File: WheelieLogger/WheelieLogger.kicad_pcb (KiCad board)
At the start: 2 copper layers, 28.8 x 22 mm, 34 parts, among them J1 USB_C_Plug_USB2.0, J2 Conn_Power, J3 Conn_GPIO, SW1 SW_RESET, U1 GD25Q32CNIGR, U2 MCP1700-3302E_SOT23, U3 ATSAMD21E18A, U4 MPU-6050

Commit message: Draft of SerpenteR2 board instructions
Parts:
- removed J3: Conn_GPIO, Connector_PinHeader_2.54mm_Extra:PinHeader_1x06_P2.54mm_Vertical_Castellated
- added SW2: SW_DIP_x02, Package_DIP:SMDIP-4_W7.62mm, F.Cu at (155.0, 88.3)
- J2: footprint Connector_PinHeader_2.54mm_Extra:PinHeader_1x04_P2.54mm_Vertical_Castellated -> Connector_JST:JST_PH_B2B-PH-SM4-TB_1x02-1MP_P2.00mm_Vertical
- moved R5 13.8 mm to (151.4, 78.7), turned to 180 degrees
- moved D3 11.0 mm to (142.1, 98.0)
- moved R1 11.0 mm to (140.6, 95.0)
- moved R2 11.0 mm to (142.1, 95.0)
- moved R3 11.0 mm to (143.6, 95.0)
- moved R7 10.8 mm to (151.4, 80.2)
- moved J2 6.94 mm to (155.0, 96.0), turned to 0 degrees
- moved D2 6.63 mm to (146.8, 98.0)
- moved D1 6.54 mm to (146.8, 96.0)
- moved C8 6.29 mm to (158.6, 81.8), turned to -90 degrees
- moved C6 4.22 mm to (151.4, 81.7), turned to 180 degrees
- moved C5 3.61 mm to (151.4, 84.7), turned to 0 degrees
- moved C7 3.17 mm to (151.4, 83.2), turned to 180 degrees
- moved U4 2.44 mm to (155.2, 81.5), turned to -90 degrees
- moved C1 1.92 mm to (147.7, 94.0), turned to 180 degrees
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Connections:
- J2 pad 1: VIN -> /PWR_SW
- J2 pad 2: VBUS -> GND
- U3 pad 5: /GPIO0 -> Net-(U3-Pad5)
- U3 pad 6: /GPIO1 -> Net-(U3-Pad6)
- U3 pad 7: /GPIO2 -> Net-(U3-Pad7)
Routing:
- net Net-(U3-Pad5): track 0.00 -> 10.9 mm
- net /GPIO0: track 10.9 -> 0.00 mm
- net /PWR_SW: track 0.00 -> 10.3 mm
- net VIN: track 9.98 -> 0.00 mm
- net /LED_B: track 23.1 -> 33.1 mm
- net Net-(U3-Pad7): track 0.00 -> 9.39 mm
- net /GPIO2: track 9.39 -> 0.00 mm
- net Net-(U3-Pad6): track 0.00 -> 9.30 mm
- net /GPIO1: track 9.30 -> 0.00 mm
- net GND: track 23.1 -> 15.2 mm
- net +3V3: track 63.9 -> 61.5 mm
- net Net-(C7-Pad1): vias 0 -> 1
- net /GPIO4: vias 1 -> 0

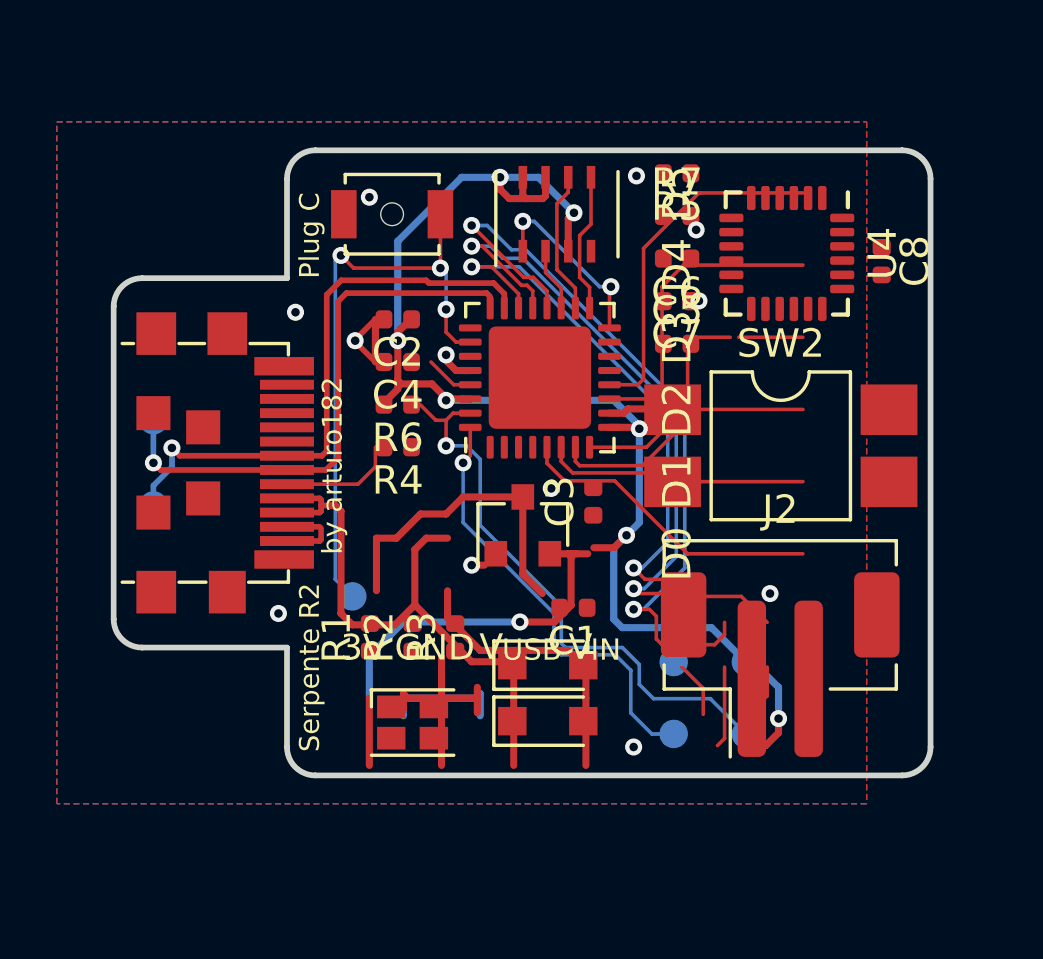
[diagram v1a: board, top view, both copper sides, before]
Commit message: 1.Added 1uF cap to pin2 of the MCP1700 (U2) 2.Removed dip switches, replaced with DPDT slide switch as they should always operate together 3.Updated the JST-PH connector from an SMD to a through-hole unit 4.Updated the footprint of the USB-C connector
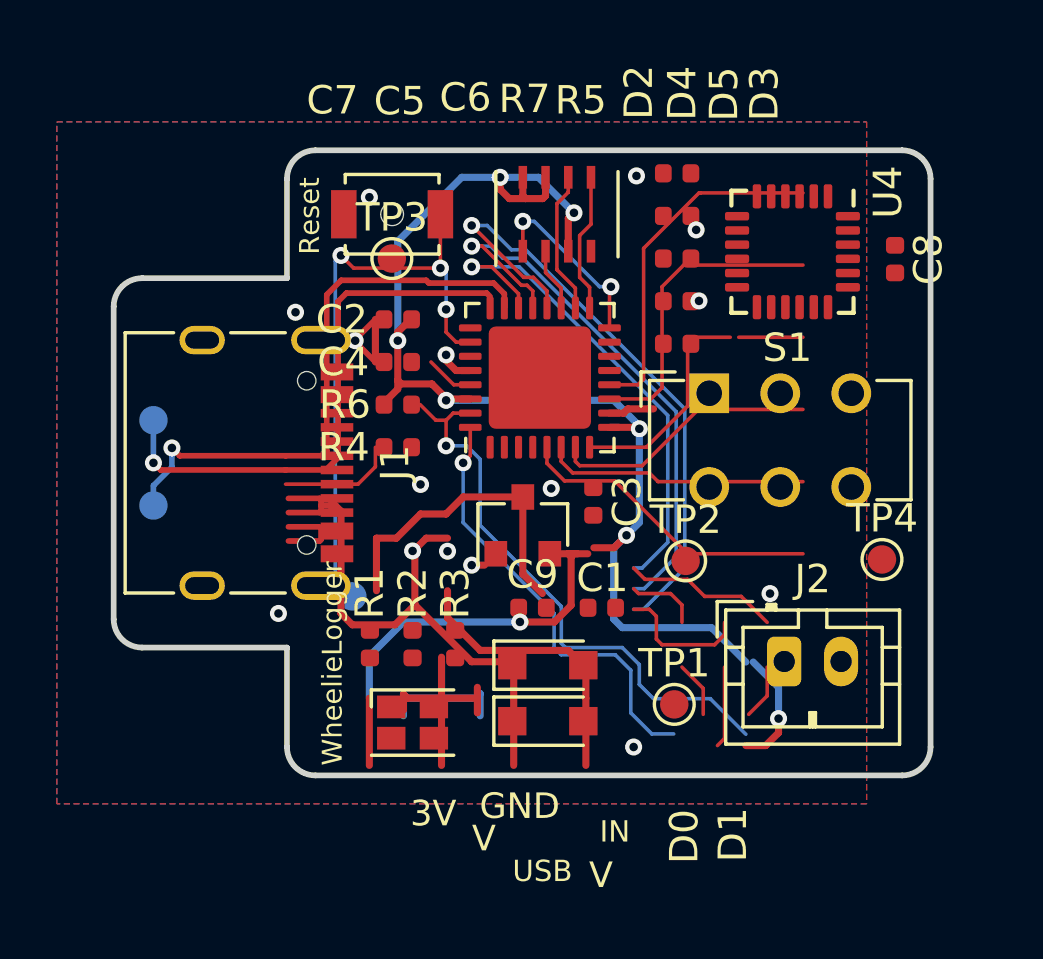
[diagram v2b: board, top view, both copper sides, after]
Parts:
- removed SW2: SW_DIP_x02, Package_DIP:SMDIP-4_W7.62mm
- added C9: 1uF, Capacitor_SMD:C_0402_1005Metric, F.Cu at (146.3, 94.0)
- added S1: JS202011JCQN, Button_Switch_THT:SW_CuK_JS202011CQN_DPDT_Straight, F.Cu at (152.5, 86.5)
- J1: footprint Connector_USB_Extra:USB_C_Plug_UTC009-C12 -> Connector_USB:USB_C_Receptacle_XKB_U262-16XN-4BVC11
- J2: footprint Connector_JST:JST_PH_B2B-PH-SM4-TB_1x02-1MP_P2.00mm_Vertical -> Connector_JST:JST_PH_B2B-PH-K_1x02_P2.00mm_Vertical
- TP1, TP2, TP3, TP4: moved to F.Cu
- moved TP3 18.9 mm to (141.3, 81.7), turned to 0 degrees
- moved TP4 8.17 mm to (158.6, 92.3), turned to 0 degrees
- moved TP2 6.10 mm to (151.7, 92.3), turned to 0 degrees
- moved TP1 2.73 mm to (151.3, 97.4), turned to 0 degrees
- moved J1 1.71 mm to (135.7, 88.9)
- moved C1 1.00 mm to (148.7, 94.0)
- moved C8 0.48 mm to (159.1, 81.7)
- moved R1 0.24 mm to (140.6, 95.3)
- moved R2 0.24 mm to (142.1, 95.3)
- moved R3 0.24 mm to (143.6, 95.3)
- moved U4 0.21 mm to (155.4, 81.5)
- moved J2 0.18 mm to (155.2, 95.9)
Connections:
- U2 pad 2: +3V3 -> Net-(C9-Pad2)
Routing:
- net +3V3: track 61.5 -> 44.6 mm, vias 9 -> 7
- net /PWR_SW: track 10.3 -> 24.5 mm, vias 0 -> 2
- net Net-(C9-Pad2): track 0.00 -> 12.8 mm, vias 0 -> 1
- net /LED_B: track 33.1 -> 27.6 mm
- net VBUS: track 21.3 -> 24.0 mm
- net GND: track 15.2 -> 12.5 mm, vias 10 -> 9
- net /LED_R: track 22.6 -> 20.1 mm, vias 2 -> 1
- net Net-(D3-Pad2): track 1.93 -> 0.00 mm
- net +5V: vias 0 -> 1
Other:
- board text added: "Reset"
- board text added: "WheelieLogger"
- board text removed: "Plug C"
- board text removed: "Serpente R2"
- board text removed: "by arturo182"

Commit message: Rebuilt the tracks in the PCB Removed some test points
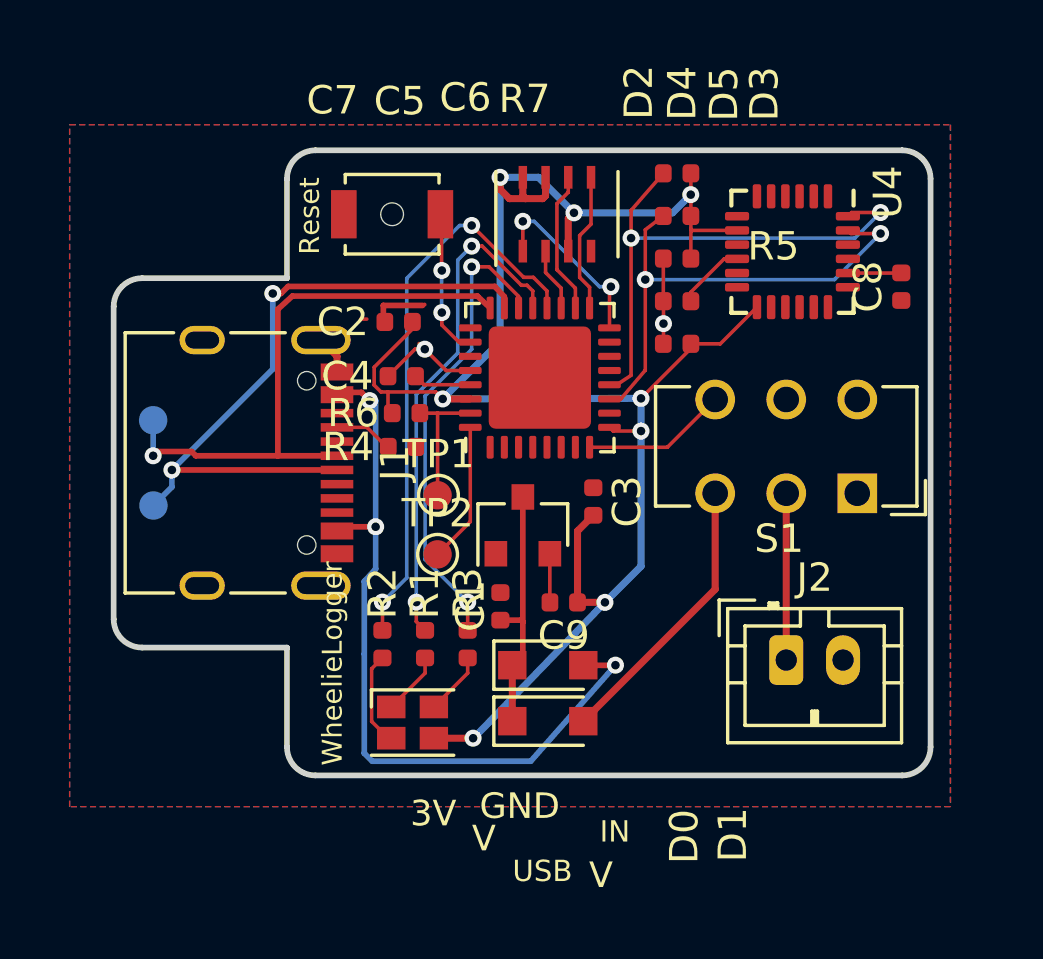
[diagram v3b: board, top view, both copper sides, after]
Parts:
- removed TP3: TP_VDD, TestPoint:TestPoint_Pad_D1.0mm
- removed TP4: TP_GND, TestPoint:TestPoint_Pad_D1.0mm
- removed TP7: TP_RESET, TestPoint:TestPoint_Pad_D1.0mm
- moved TP1 11.1 mm to (143.0, 90.0)
- moved TP2 8.73 mm to (142.9, 92.1)
- moved S1 6.29 mm to (157.7, 90.0), turned to 180 degrees
- moved C1 3.57 mm to (145.2, 94.0), turned to -90 degrees
- moved R1 1.94 mm to (142.5, 95.3)
- moved C9 1.12 mm to (147.4, 93.8), turned to 180 degrees
- moved R2 1.06 mm to (141.0, 95.3)
- moved C8 0.99 mm to (159.3, 82.7), turned to 90 degrees
- moved C4 0.52 mm to (141.7, 85.8)
- moved R3 0.44 mm to (144.0, 95.3)
- moved R6 0.42 mm to (141.8, 87.2)
- moved R4 0.15 mm to (141.7, 88.3)
- moved C2 0.09 mm to (141.6, 83.9)
- moved J2 0.09 mm to (155.2, 95.8)
- turned R5 to 0 degrees
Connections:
- S1 pad 2: VIN -> /PWR_SW
- S1 pad 3: /PWR_SW -> VIN
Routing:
- net +3V3: track 44.6 -> 67.3 mm, vias 7 -> 8
- net /PWR_SW: track 24.5 -> 5.87 mm, vias 2 -> 0
- net /~RESET~: track 21.2 -> 5.22 mm, vias 3 -> 2
- net Net-(R6-Pad1): track 20.4 -> 4.67 mm, vias 1 -> 0
- net /LED_B: track 27.6 -> 16.6 mm
- net Net-(C9-Pad2): track 12.8 -> 1.71 mm, vias 1 -> 0
- net Net-(U3-Pad5): track 10.9 -> 0.00 mm
- net Net-(TP2-Pad1): track 15.5 -> 4.95 mm, vias 1 -> 0
- net VIN: track 0.00 -> 9.94 mm
- net Net-(U3-Pad7): track 9.39 -> 0.00 mm
- net Net-(U3-Pad6): track 9.30 -> 0.00 mm
- net /LED_G: track 27.1 -> 20.0 mm
- net /GPIO4: track 10.8 -> 17.6 mm, vias 0 -> 2
- net /GPIO5: track 12.3 -> 18.7 mm, vias 0 -> 2
- net /GPIO3: track 10.1 -> 5.12 mm
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
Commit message: Improved bottom layer GND mask Added part numbers for D1 and D2 Tidy up top and bottom silk screen layers
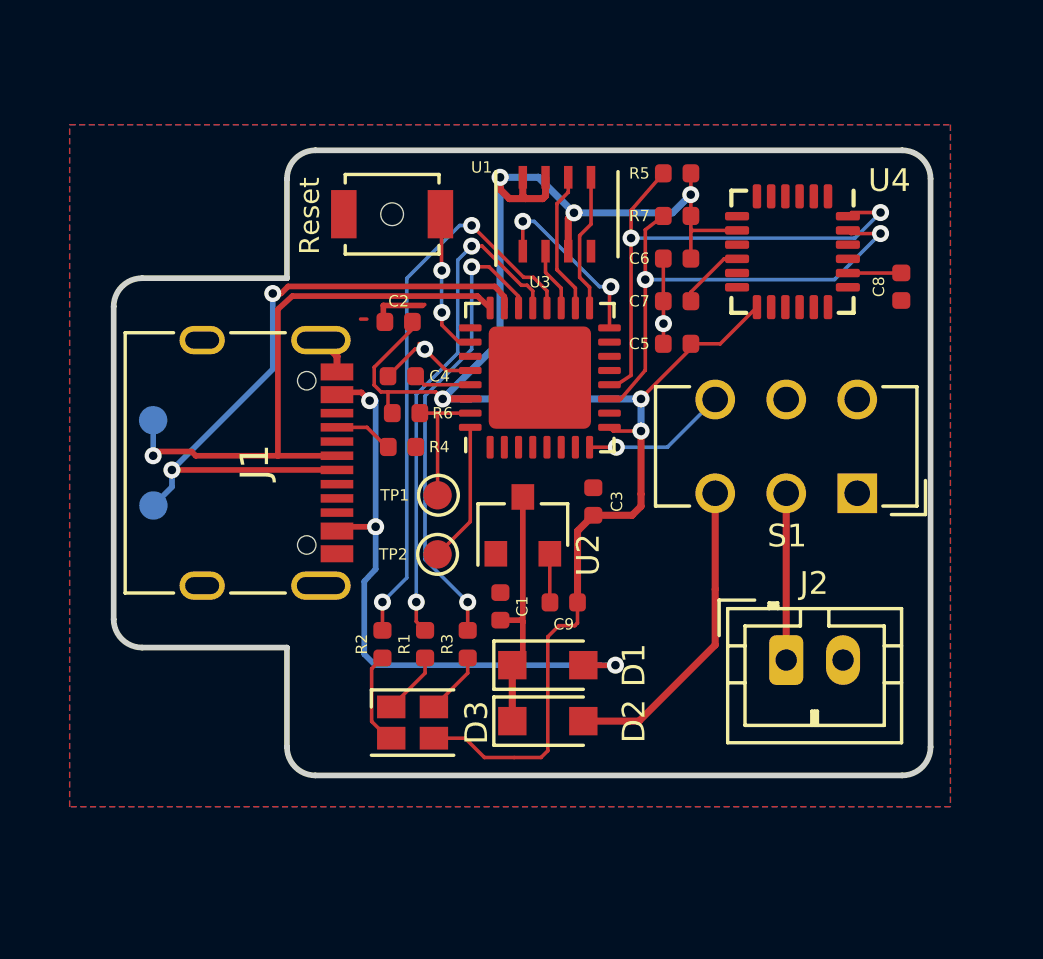
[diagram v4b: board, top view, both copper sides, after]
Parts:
- removed G***: LOGO, serpente:qrcode
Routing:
- net VBUS: track 27.1 -> 22.1 mm
- net VIN: track 9.94 -> 11.1 mm
- net +3V3: track 67.3 -> 66.4 mm, vias 8 -> 6
- net /GPIO3: vias 0 -> 1
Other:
- board text added: "J2"
- board text added: "S1A"
- board text added: "S1B"
- board text added: "WheelieLogger v1.0"
- board text removed: "3V"
- board text removed: "CLK"
- board text removed: "D0"
- board text removed: "D1"
- board text removed: "D2"
- board text removed: "D3"
- board text removed: "D4"
- board text removed: "D5"
- board text removed: "DAT"
- board text removed: "GND"
- board text removed: "IN"
- board text removed: "USB"
- board text removed: "V"
- board text removed: "WheelieLogger"

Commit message: Added J-link connector Moved the diodes to make room for it
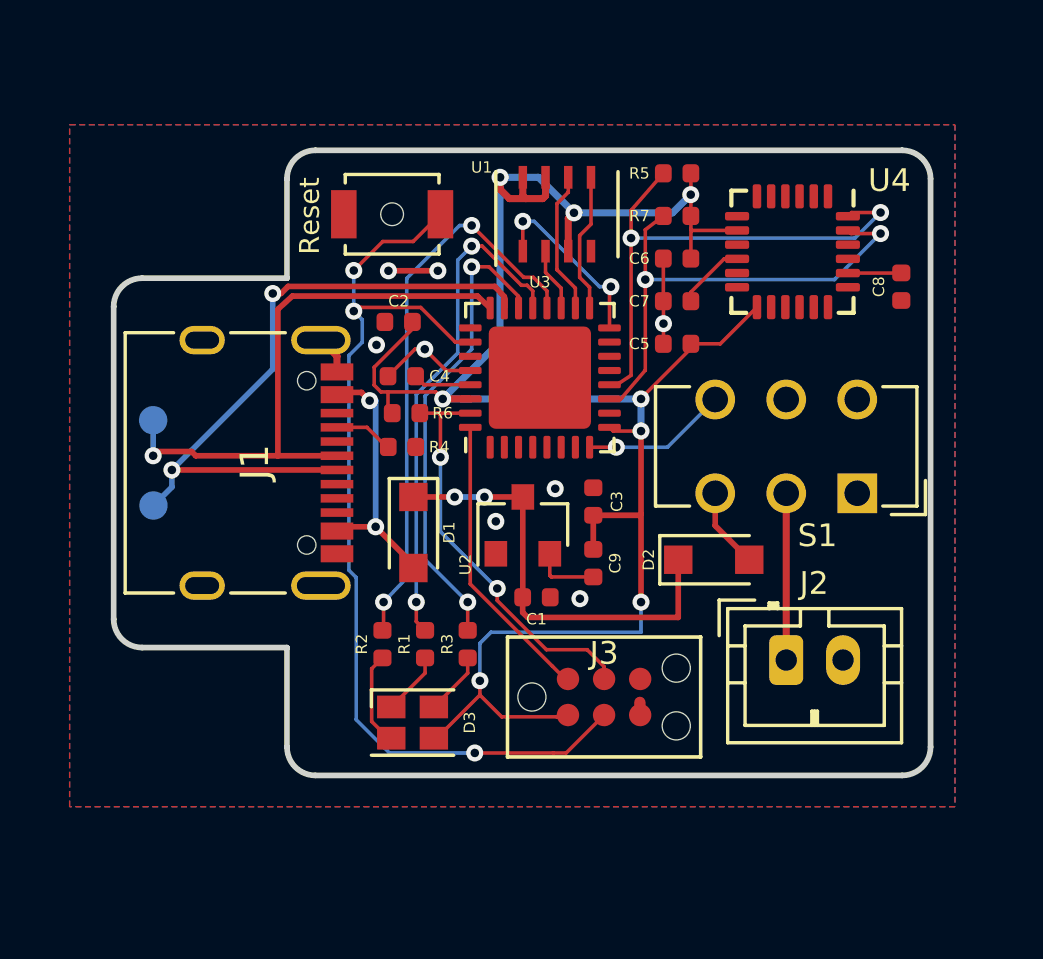
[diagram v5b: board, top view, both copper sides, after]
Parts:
- removed TP1: TP_SWCLK, TestPoint:TestPoint_Pad_D1.0mm
- removed TP2: TP_SWDIO, TestPoint:TestPoint_Pad_D1.0mm
- added J3: TC2030-IDC-NL, TC2030:TAG_TC2030-IDC-NL, F.Cu at (148.8, 97.1)
- moved D2 8.15 mm to (152.7, 92.3)
- moved D1 6.65 mm to (142.1, 91.3), turned to -90 degrees
- moved C9 1.73 mm to (148.4, 92.4), turned to -90 degrees
- moved C1 1.31 mm to (146.4, 93.6), turned to 180 degrees
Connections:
- net Net-(R6-Pad1) renamed /SWCLK
- U3 pad 32: Net-(TP2-Pad1) -> /SWDIO
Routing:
- net /~RESET~: track 5.22 -> 34.7 mm, vias 2 -> 3
- net VBUS: track 22.1 -> 9.38 mm, vias 3 -> 2
- net /SWDIO: track 0.00 -> 10.3 mm
- net /SWCLK: track 4.67 -> 14.4 mm, vias 0 -> 2
- net VIN: track 11.1 -> 2.84 mm
- net +5V: track 9.25 -> 15.5 mm, vias 0 -> 2
- net +3V3: track 66.4 -> 71.8 mm, vias 6 -> 8
- net Net-(TP2-Pad1): track 4.95 -> 0.00 mm
- net Net-(C9-Pad2): track 1.71 -> 2.31 mm
- net GND: vias 2 -> 8

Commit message: Updated to version 2
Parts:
- added C10: 1uF, Capacitor_SMD:C_0402_1005Metric, F.Cu at (150.1, 91.7)
- added C11: 1uF, Capacitor_SMD:C_0402_1005Metric, F.Cu at (152.0, 85.3)
- added D4: Red, LED_SMD:LED_0402_1005Metric, F.Cu at (154.0, 85.3)
- added D5: Yellow, LED_SMD:LED_0402_1005Metric, F.Cu at (152.2, 91.7)
- added D6: Green, LED_SMD:LED_0402_1005Metric, F.Cu at (154.5, 91.7)
- added R10: 1.5kR, Resistor_SMD:R_0402_1005Metric, F.Cu at (153.4, 91.7)
- added R8: 1.5kR, Resistor_SMD:R_0402_1005Metric, F.Cu at (153.0, 85.3)
- added R9: 1.5kR, Resistor_SMD:R_0402_1005Metric, F.Cu at (151.2, 91.7)
- added U5: MCP73833-AMI_UN, Footprints:SON50P300X300X100-11N, F.Cu at (152.3, 88.5)
- J3: footprint TC2030:TAG_TC2030-IDC-NL -> Footprints:Tag-Connect_TC2030-IDC-NL
- S1: footprint Button_Switch_THT:SW_CuK_JS202011CQN_DPDT_Straight -> Footprints:SW_JS202011JCQN
- moved D2 2.75 mm to (150.6, 94.2)
- moved J3 1.54 mm to (147.5, 97.9)
- moved S1 0.98 mm to (157.4, 89.0), turned to 0 degrees
- moved C5 0.75 mm to (150.9, 85.3), turned to -90 degrees
- moved C8 0.64 mm to (159.3, 82.1)
- moved U4 0.64 mm to (155.4, 80.8)
- moved C9 0.27 mm to (148.3, 92.2)
- moved J2 0.22 mm to (155.2, 96.1)
- moved C3 0.14 mm to (148.3, 90.2)
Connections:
- C9 pad 1: +3V3 -> GND
- C9 pad 2: Net-(C9-Pad2) -> +3V3
- S1 pad 1: Net-(S1-Pad1) -> /GPIO3
- S1 pad 2: /PWR_SW -> GND
- S1 pad 3: VIN -> Net-(S1-Pad3)
- S1 pad 5: GND -> /PWR_SW
- S1 pad 6: /GPIO3 -> VIN
- U2 pad 2: Net-(C9-Pad2) -> +3V3
- U4 pad 9: Net-(U4-Pad9) -> +3V3
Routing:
- net VIN: track 2.84 -> 10.2 mm
- net /PWR_SW: track 5.87 -> 13.2 mm
- net /GPIO3: track 5.12 -> 10.7 mm, vias 1 -> 2
- net +3V3: track 71.8 -> 67.1 mm
- net +5V: track 15.5 -> 18.9 mm
- net Net-(C9-Pad2): track 2.31 -> 0.00 mm
- net Net-(R9-Pad1): track 0.00 -> 2.00 mm
- net Net-(C8-Pad2): track 1.89 -> 0.00 mm
- net Net-(R10-Pad1): track 0.00 -> 1.55 mm
- net Net-(D6-Pad1): track 0.00 -> 1.50 mm
- net Net-(D5-Pad1): track 0.00 -> 1.47 mm
- net Net-(R8-Pad1): track 0.00 -> 1.31 mm
- net GND: track 10.2 -> 10.8 mm
